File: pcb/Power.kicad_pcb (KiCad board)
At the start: 2 copper layers, 16.2 x 36 mm, 15 parts, among them P1 CONN_02X10, P2 CONN_01X05, P4 CONN_01X02

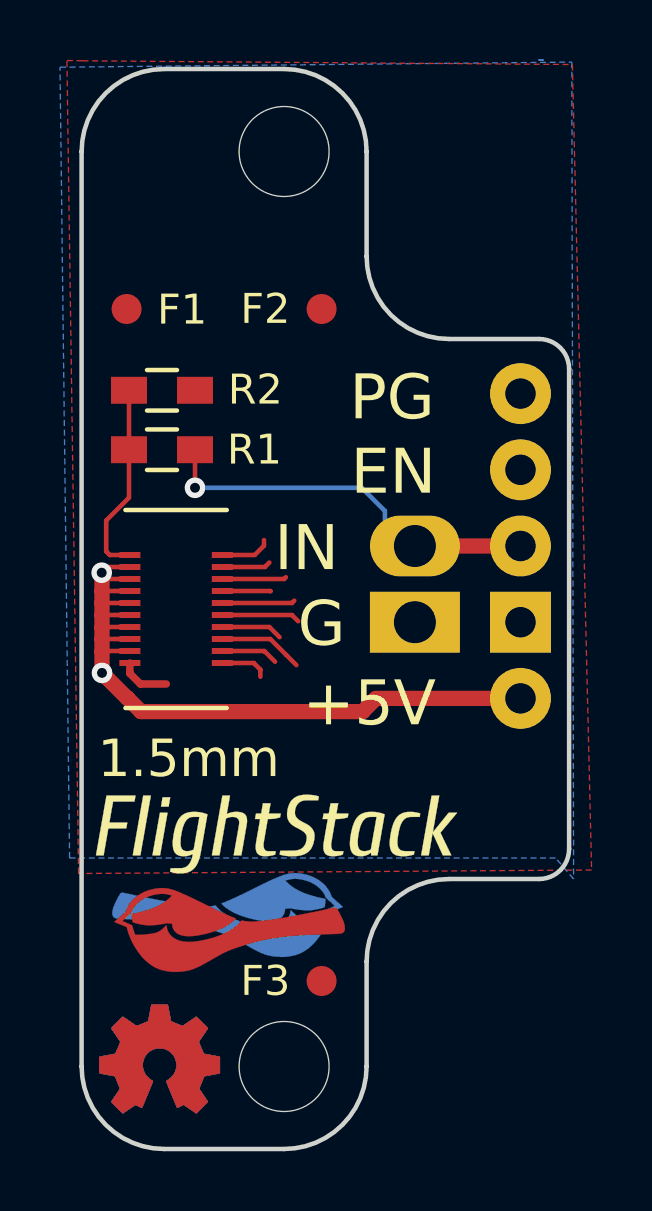
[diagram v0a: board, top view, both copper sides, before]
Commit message: Rebrand everything to Polystack and increment versions.
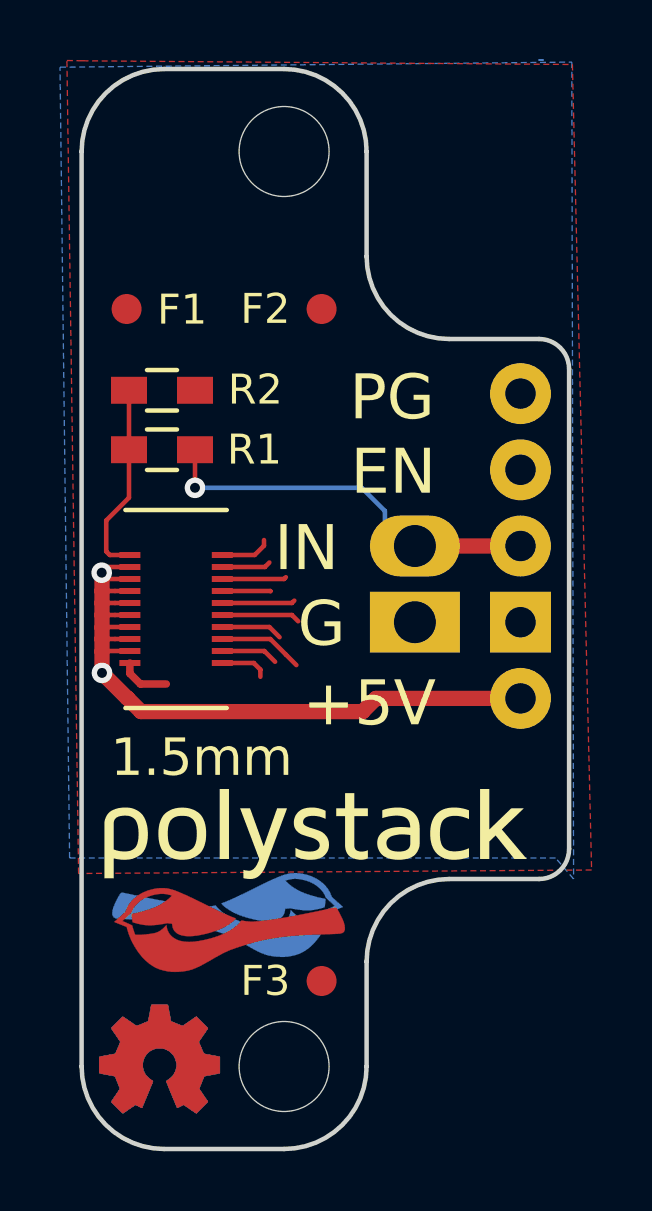
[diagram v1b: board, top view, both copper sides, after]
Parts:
- removed the G*** at (163.0, 115.5)
- added svg2mod: G***, polystack:polystack-medium-0.75, B.Cu at (164.3, 114.8)
- added svg2mod: G***, polystack:polystack-medium-0.75, F.Cu at (164.3, 115.5)
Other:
- rule pad_to_mask_clearance: 0.2 -> 0.0762
- board text added: "ckd.tech/p-p/v6"
- board text removed: "ckd.tech/p-p/v5"

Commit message: Update polystack logo to bold variant and bump version number.
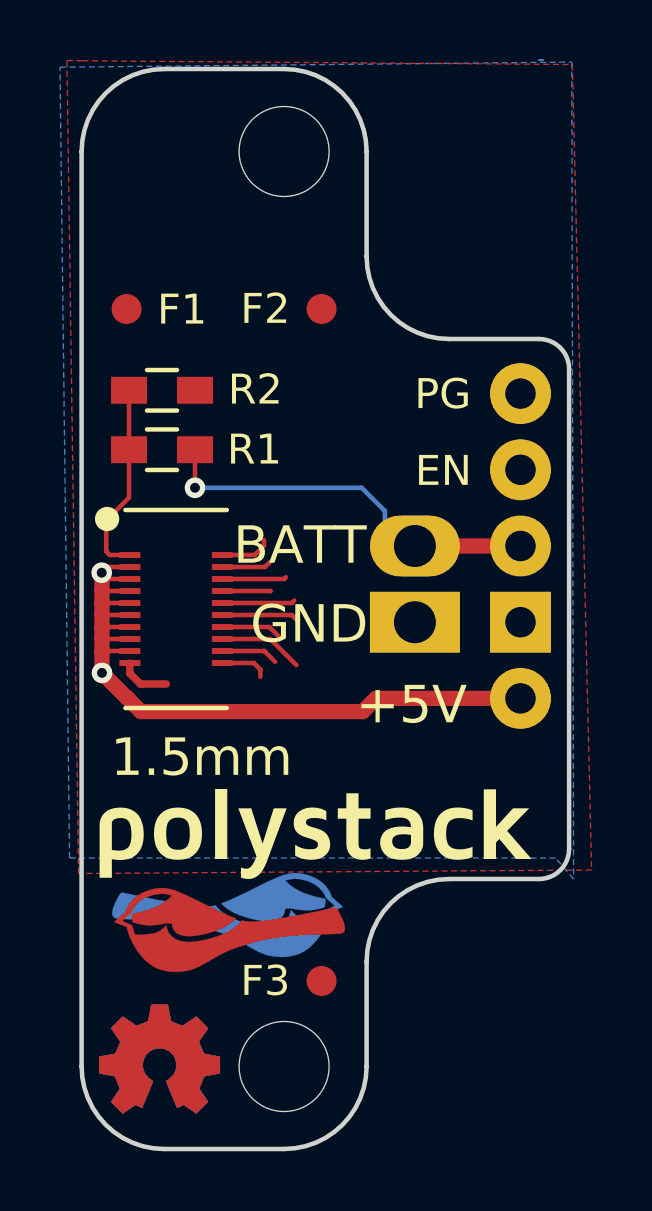
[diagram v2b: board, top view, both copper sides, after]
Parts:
- svg2mod (x2): footprint polystack:polystack-medium-0.75 -> polystack:polystack-bold-0.75
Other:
- board text added: "BATT"
- board text added: "ckd.tech/p-p/v7"
- board text removed: "G"
- board text removed: "IN"
- board text removed: "ckd.tech/p-p/v6"

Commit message: Add license information to many files. PCB design files are CC-BY and code is MIT license.
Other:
- board text added: "Copyright 2016 Chickadee Tech LLC This work is licensed under the Creative Commons Attribution 4.0 International License. To view a copy of this license, visit http://creativecommons.org/licenses/by/4.0/ or send a letter to Creative Commons, PO Box 1866, Mountain View, CA 94042, USA."
- board text added: "Remove all Chickadee Tech LLC trademarks before making your own board. The Chickadee logo and Polystack logo are owned by Chickadee Tech LLC. You may license the Polystack logo for free by emailing support@chickadee.tech and receiving express written permission from Chickadee Tech LLC."
- board text added: "The gear logo is a mark designating open source hardware. Remove it if your design does not comply with the open source hardware definition."
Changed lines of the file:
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@@
     (links 25)
     (no_connects 0)
-    (area 156.424999 89.924999 172.825001 126.075001)
+    (area 131.277143 85.19 262.310001 185.82)
     (thickness 1.6)
-    (drawings 37)
+    (drawings 43)
     (tracks 72)
     (zones 0)
@@
     (40 Dwgs.User user)
     (41 Cmts.User user)
-    (42 Eco1.User user hide)
-    (43 Eco2.User user hide)
+    (42 Eco1.User user)
+    (43 Eco2.User user)
     (44 Edge.Cuts user)
     (45 Margin user)
@@
       (xy 5.606686 -0.833425)) (layer B.SilkS) (width 0))
   )
+  (gr_line (start 129.7 117.31) (end 156.71 118.72) (layer Cmts.User) (width 0.41))
+  (gr_line (start 156.55 115.44) (end 129.7 117.31) (layer Cmts.User) (width 0.41))
+  (gr_text "Remove all Chickadee Tech LLC trademarks\nbefore making your own board. The\nChickadee logo and Polystack logo\nare owned by Chickadee Tech LLC.\n\nYou may license the Polystack logo for\nfree by emailing support@chickadee.tech\nand receiving express written permission\nfrom Chickadee Tech LLC." (at 89.11 119.03) (layer Cmts.User)
+    (effects (font (size 1.5 1.5) (thickness 0.3)) (justify left))
+  )
+  (gr_line (start 161.4 124.28) (end 169.43 126.81) (layer Cmts.User) (width 0.41))
+  (gr_text "The gear logo is a mark designating open\nsource hardware. Remove it if your design\ndoes not comply with the open source\nhardware definition." (at 169.85 126.81) (layer Cmts.User)
+    (effects (font (size 1.5 1.5) (thickness 0.3)) (justify left))
+  )
+  (gr_text "Copyright 2016 Chickadee Tech LLC\n\nThis work is licensed under the Creative Commons Attribution 4.0 International License.\nTo view a copy of this license, visit http://creativecommons.org/licenses/by/4.0/\nor send a letter to Creative Commons, PO Box 1866, Mountain View, CA 94042, USA.\n" (at 160.66 179.82) (layer Cmts.User)
+    (effects (font (size 1.5 1.5) (thickness 0.3)) (justify left))
+  )
   (gr_circle (center 157.35 105) (end 157.55 105) (layer F.SilkS) (width 0.41))
